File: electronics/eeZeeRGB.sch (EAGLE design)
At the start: 5 parts

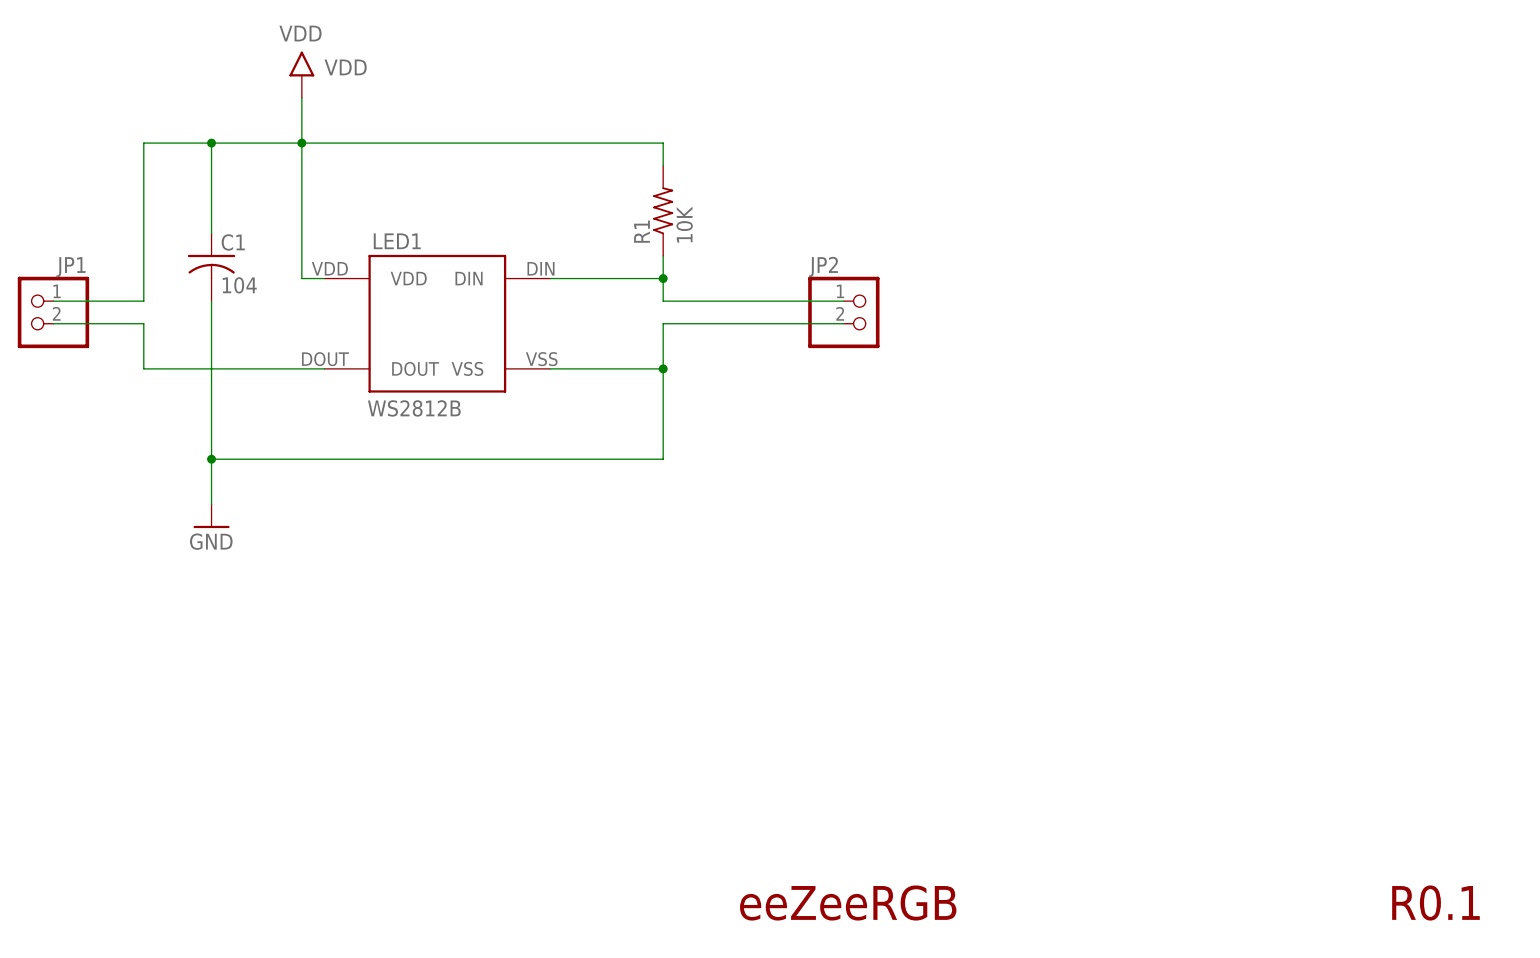
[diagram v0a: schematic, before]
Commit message: added solder jumper to disable 10k pullup, moved passives layout, minor silk changes, changed silk for ws2812b
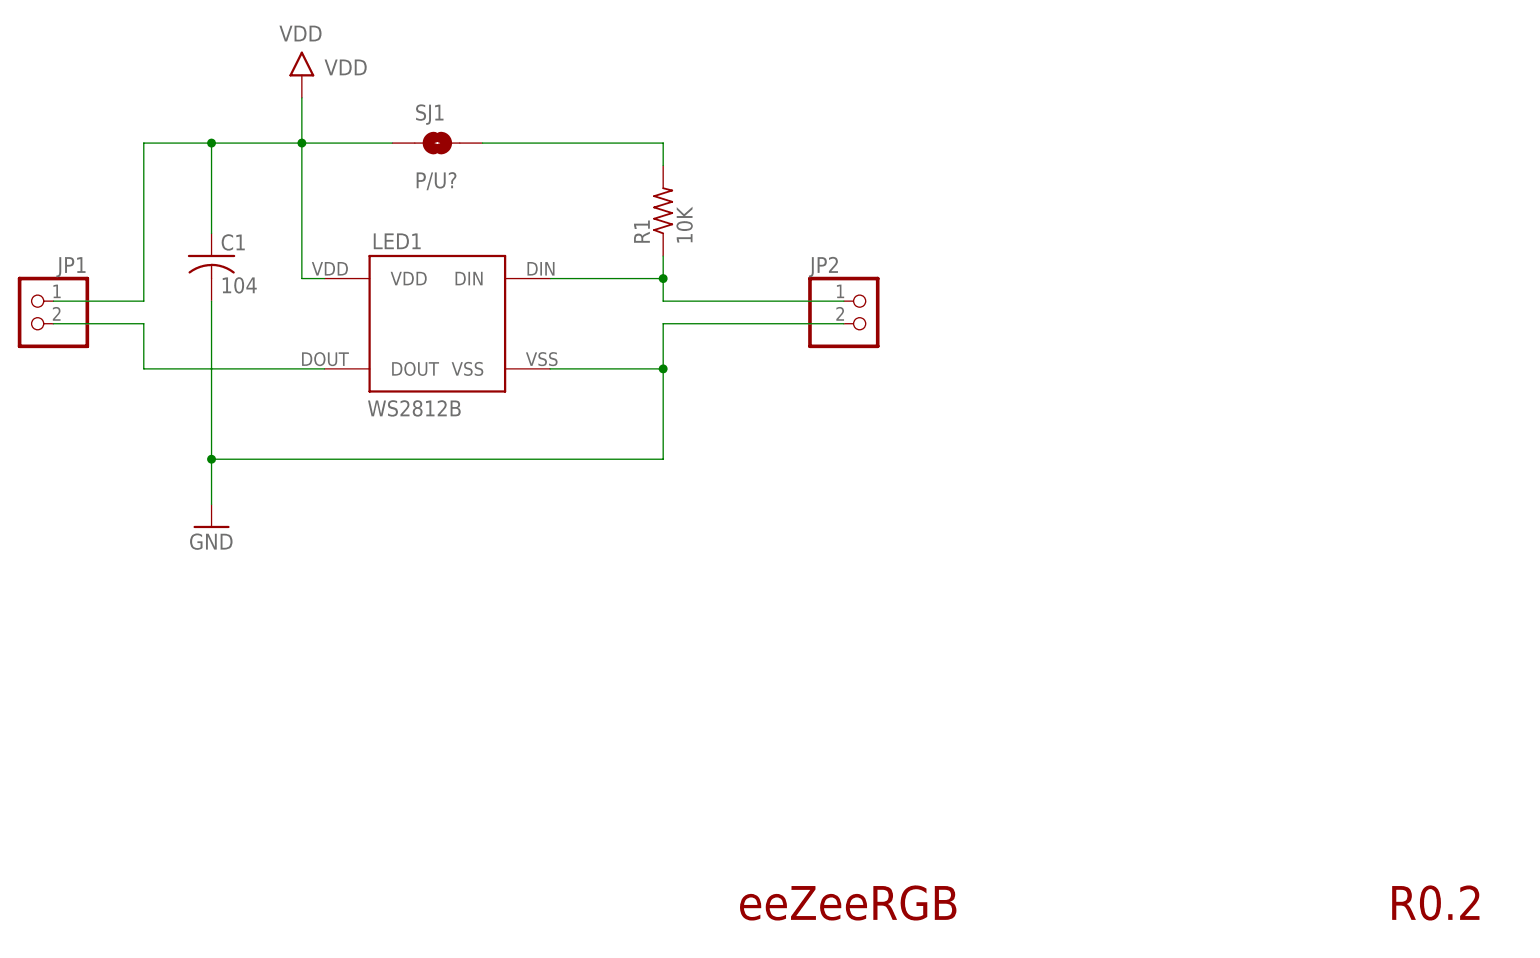
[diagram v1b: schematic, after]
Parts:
- added SJ1: P/U?, SparkFun-Retired:SOLDERJUMPER-OLDNC
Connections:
- new net N$1: R1.2, SJ1.2
- net VDD: now also SJ1.1; no longer R1.2
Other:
- note added: "R0.2"
- note removed: "R0.1"
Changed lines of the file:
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@@
 <?xml version="1.0" encoding="utf-8"?>
 <!DOCTYPE eagle SYSTEM "eagle.dtd">
-<eagle version="6.4">
+<eagle version="7.1.0">
 <drawing>
 <settings>
@@
 <layer number="54" name="bPadExt" color="1" fill="1" visible="no" active="no"/>
 <layer number="56" name="wert" color="7" fill="1" visible="no" active="no"/>
+<layer number="57" name="tCAD" color="7" fill="1" visible="no" active="no"/>
+<layer number="59" name="tCarbon" color="7" fill="1" visible="no" active="no"/>
+<layer number="60" name="bCarbon" color="7" fill="1" visible="no" active="no"/>
+<layer number="90" name="Modules" color="5" fill="1" visible="no" active="no"/>
 <layer number="91" name="Nets" color="2" fill="1" visible="yes" active="yes"/>
 <layer number="92" name="Busses" color="1" fill="1" visible="yes" active="yes"/>
@@
 <layer number="97" name="Info" color="7" fill="1" visible="yes" active="yes"/>
 <layer number="98" name="Guide" color="6" fill="1" visible="yes" active="yes"/>
+<layer number="99" name="SpiceOrder" color="7" fill="1" visible="no" active="no"/>
 <layer number="100" name="NonViaHole" color="14" fill="1" visible="no" active="yes"/>
 <layer number="101" name="PlacementGuide" color="7" fill="1" visible="no" active="yes"/>
@@
 <layer number="106" name="bPlate" color="7" fill="1" visible="no" active="yes"/>
 <layer number="107" name="Crop" color="7" fill="1" visible="no" active="yes"/>
+<layer number="108" name="tplace-old" color="10" fill="1" visible="no" active="yes"/>
+<layer number="109" name="ref-old" color="11" fill="1" visible="no" active="yes"/>
+<layer number="110" name="fp0" color="7" fill="1" visible="no" active="yes"/>
+<layer number="111" name="LPC17xx" color="7" fill="1" visible="no" active="yes"/>
+<layer number="112" name="tSilk" color="7" fill="1" visible="yes" active="yes"/>
+<layer number="113" name="IDFDebug" color="4" fill="1" visible="no" active="yes"/>
 <layer number="116" name="Patch_BOT" color="9" fill="4" visible="no" active="yes"/>
 <layer number="121" name="_tsilk" color="7" fill="1" visible="no" active="yes"/>
 <layer number="122" name="_bsilk" color="7" fill="1" visible="no" active="yes"/>
+<layer number="123" name="tTestmark" color="7" fill="1" visible="no" active="yes"/>
+<layer number="124" name="bTestmark" color="7" fill="1" visible="no" active="yes"/>
 <layer number="125" name="_tNames" color="7" fill="1" visible="no" active="yes"/>
+<layer number="126" name="_bNames" color="7" fill="1" visible="no" active="yes"/>
+<layer number="127" name="_tValues" color="7" fill="1" visible="no" active="yes"/>
+<layer number="128" name="_bValues" color="7" fill="1" visible="no" active="yes"/>
+<layer number="129" name="Mask" color="7" fill="1" visible="no" active="yes"/>
+<layer number="131" name="tAdjust" color="7" fill="1" visible="no" active="yes"/>
+<layer number="132" name="bAdjust" color="7" fill="1" visible="no" active="yes"/>
 <layer number="144" name="Drill_legend" color="7" fill="1" visible="no" active="yes"/>
+<layer number="150" name="Notes" color="7" fill="1" visible="no" active="yes"/>
 <layer number="151" name="HeatSink" color="7" fill="1" visible="no" active="yes"/>
+<layer number="152" name="_bDocu" color="7" fill="1" visible="no" active="yes"/>
+<layer number="153" name="FabDoc1" color="7" fill="1" visible="no" active="yes"/>
+<layer number="154" name="FabDoc2" color="7" fill="1" visible="no" active="yes"/>
+<layer number="155" name="FabDoc3" color="7" fill="1" visible="no" active="yes"/>
+<layer number="199" name="Contour" color="7" fill="1" visible="no" active="yes"/>
 <layer number="200" name="200bmp" color="1" fill="10" visible="no" active="yes"/>
 <layer number="201" name="201bmp" color="2" fill="10" visible="no" active="yes"/>
@@
 <layer number="223" name="223bmp" color="24" fill="1" visible="no" active="no"/>
 <layer number="224" name="224bmp" color="25" fill="1" visible="no" active="no"/>
+<layer number="225" name="225bmp" color="7" fill="1" visible="no" active="yes"/>
+<layer number="226" name="226bmp" color="7" fill="1" visible="no" active="yes"/>
+<layer number="227" name="227bmp" color="7" fill="1" visible="no" active="yes"/>
+<layer number="228" name="228bmp" color="7" fill="1" visible="no" active="yes"/>
+<layer number="229" name="229bmp" color="7" fill="1" visible="no" active="yes"/>
+<layer number="230" name="230bmp" color="7" fill="1" visible="no" active="yes"/>
 <layer number="231" name="Eagle3D_PG1" color="14" fill="1" visible="no" active="yes"/>
 <layer number="232" name="Eagle3D_PG2" color="14" fill="2" visible="no" active="yes"/>
 <layer number="233" name="Eagle3D_PG3" color="14" fill="4" visible="no" active="yes"/>
+<layer number="248" name="Housing" color="7" fill="1" visible="no" active="yes"/>
+<layer number="249" name="Edge" color="7" fill="1" visible="no" active="yes"/>
 <layer number="250" name="Descript" color="7" fill="1" visible="no" active="yes"/>
 <layer number="251" name="SMDround" color="7" fill="1" visible="no" active="yes"/>
 <layer number="254" name="OrgLBR" color="7" fill="1" visible="no" active="yes"/>
+<layer number="255" name="routoute" color="7" fill="1" visible="no" active="yes"/>
 </layers>
 <schematic xreflabel="%F%N/%S.%C%R" xrefpart="/%S.%C%R">
@@
 <part name="GND1" library="bt" deviceset="GND" device=""/>
 <part name="FRAME1" library="bt" deviceset="LETTER_L" device=""/>
+<part name="SJ1" library="SparkFun-Retired" deviceset="SOLDERJUMPER-OLD" device="NC" value="P/U?"/>
 </parts>
 <sheets>
@@
 <plain>
 <text x="158.242" y="24.384" size="3.81" layer="94">eeZeeRGB</text>
-<text x="231.394" y="24.384" size="3.81" layer="94">R0.1</text>
+<text x="231.394" y="24.384" size="3.81" layer="94">R0.2</text>
 </plain>
 <instances>
@@
 <instance part="FRAME1" gate="G$1" x="0" y="0"/>
 <instance part="FRAME1" gate="G$2" x="147.32" y="2.54"/>
+<instance part="SJ1" gate="1" x="124.46" y="111.76"/>
 </instances>
 <busses>
@@
 <net name="VDD" class="0">
 <segment>
-<pinref part="R1" gate="G$1" pin="2"/>
 <wire x1="99.06" y1="111.76" x2="109.22" y2="111.76" width="0.1524" layer="91"/>
-<wire x1="109.22" y1="111.76" x2="149.86" y2="111.76" width="0.1524" layer="91"/>
-<wire x1="149.86" y1="111.76" x2="149.86" y2="109.22" width="0.1524" layer="91"/>
+<wire x1="109.22" y1="111.76" x2="119.38" y2="111.76" width="0.1524" layer="91"/>
 <pinref part="C1" gate="G$1" pin="1"/>
 <wire x1="99.06" y1="101.6" x2="99.06" y2="111.76" width="0.1524" layer="91"/>
@@
 <pinref part="U$1" gate="G$1" pin="VDD"/>
 <wire x1="109.22" y1="111.76" x2="109.22" y2="116.84" width="0.1524" layer="91"/>
-</segment>
-</net>
+<pinref part="SJ1" gate="1" pin="1"/>
+</segment>
+</net>
+<net name="N$1" class="0">
+<segment>
+<pinref part="R1" gate="G$1" pin="2"/>
+<pinref part="SJ1" gate="1" pin="2"/>
+<wire x1="129.54" y1="111.76" x2="149.86" y2="111.76" width="0.1524" layer="91"/>
+<wire x1="149.86" y1="111.76" x2="149.86" y2="109.22" width="0.1524" layer="91"/>
+</segment>
+</net>
